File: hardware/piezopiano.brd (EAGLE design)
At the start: 175.5 x 99.8 mm, 75 parts, among them J1 CON2, J4 JST-PH-2-SMT-SE, Q1 DMN3404L, Q2 DMN3404L, Q3 DMN3404L, Q4 DMN3404L, Q5 DMN3404L, Q6 DMN3404L, Q7 DMN3404L, Q8 DMN3404L, U2 CH340E_MSOP10, U3 TP4333, U4 MEGA328PB-AU, Y1 830069392

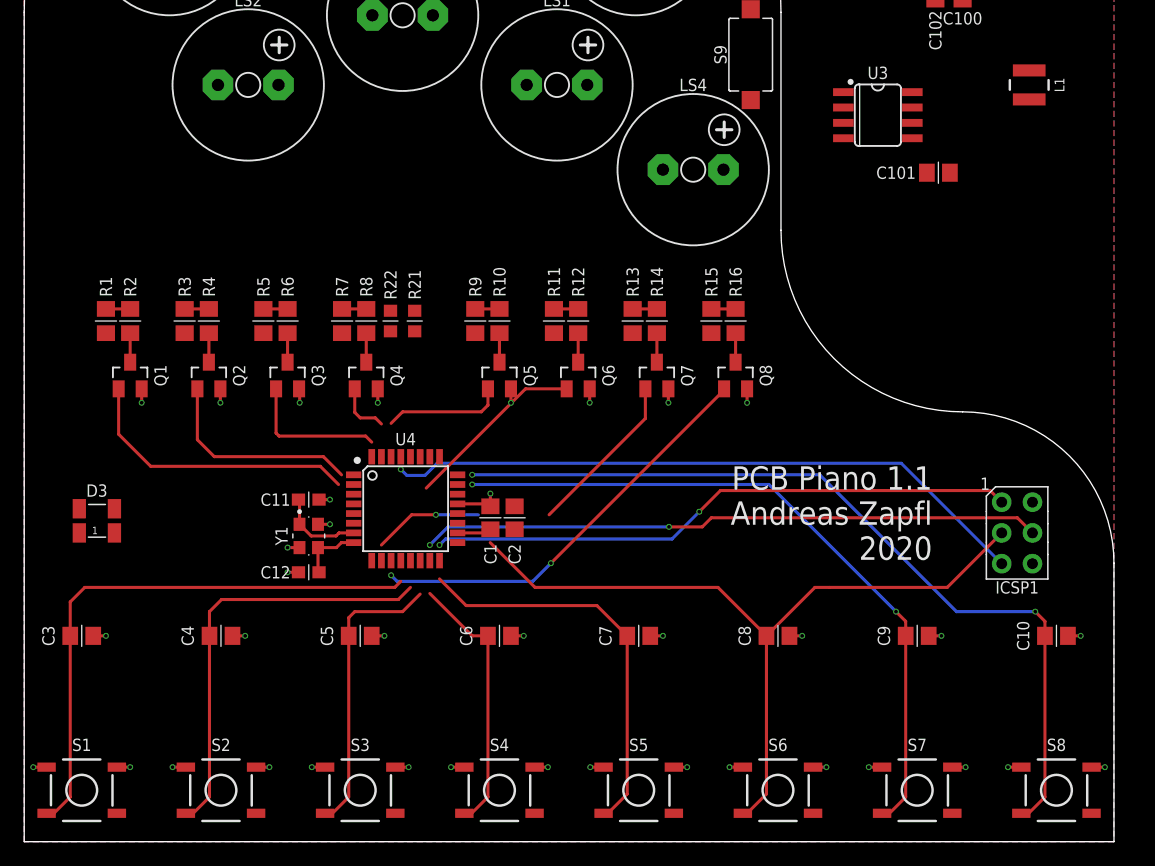
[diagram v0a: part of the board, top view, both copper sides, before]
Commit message: Added housing information and shifted piezo to be symmetric
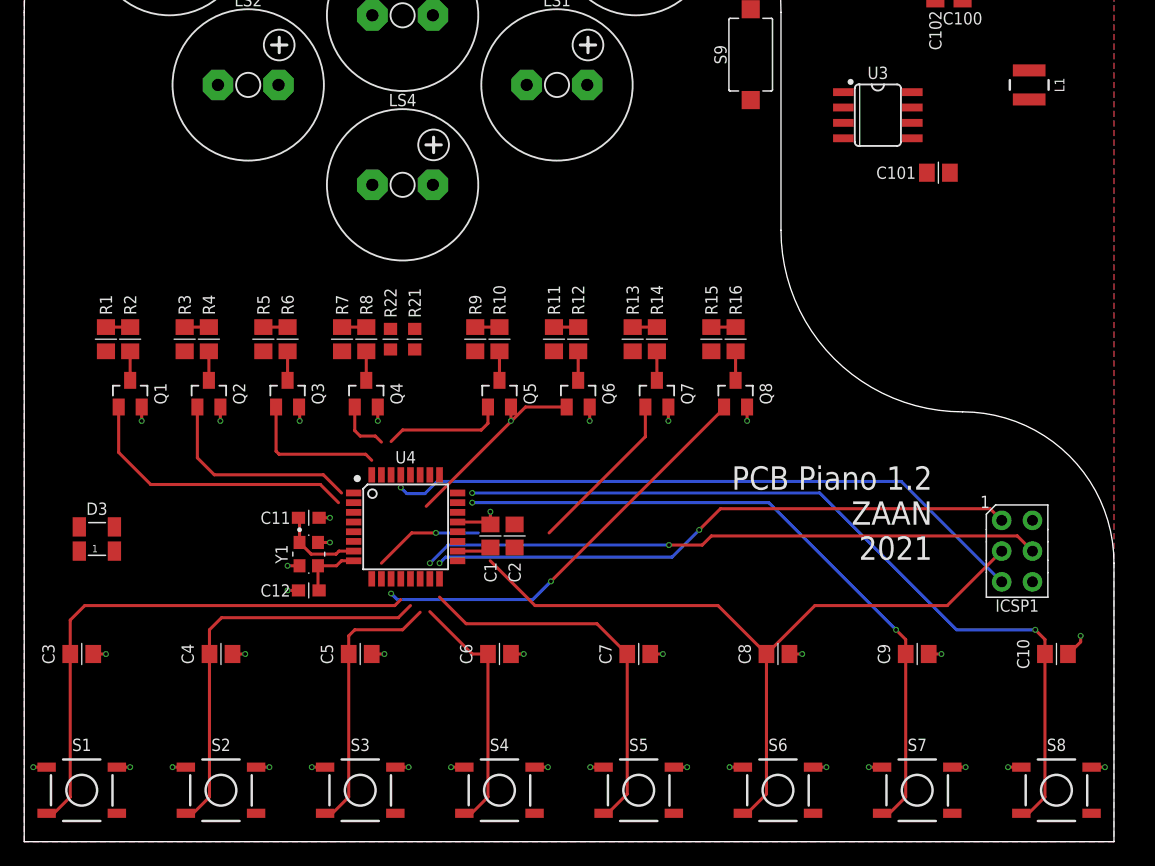
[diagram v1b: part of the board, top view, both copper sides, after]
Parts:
- moved LS4 24.0 mm to (31.2, 54.2)
- moved C1 1.50 mm to (38.5, 25.2)
- moved C10 1.50 mm to (85.2, 15.5)
- moved C11 1.50 mm to (23.5, 26.8)
- moved C12 1.50 mm to (23.5, 20.8)
- moved C2 1.50 mm to (40.5, 25.2)
- moved C3 1.50 mm to (4.75, 15.5)
- moved C4 1.50 mm to (16.2, 15.5)
- moved C5 1.50 mm to (27.8, 15.5)
- moved C6 1.50 mm to (39.2, 15.5)
- moved C7 1.50 mm to (50.8, 15.5)
- moved C8 1.50 mm to (62.2, 15.5)
- moved C9 1.50 mm to (73.8, 15.5)
- moved D3 1.50 mm to (6.00, 25.0)
- moved ICSP1 1.50 mm to (82.0, 24.0)
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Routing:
- net T7: track 64.6 -> 63.1 mm
- net T8: track 81.8 -> 80.3 mm
- net T6: track 57.5 -> 56.0 mm
- net T5: track 69.3 -> 67.8 mm
- net T4: track 46.6 -> 45.1 mm
- net T3: track 35.2 -> 33.7 mm
- net T2: track 24.0 -> 22.5 mm
- net T1: track 73.3 -> 71.8 mm
- net GND: track 42.9 -> 43.9 mm
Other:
- board text added: "PCB Piano 1.2 ZAAN 2021"
- board text removed: "PCB Piano 1.1 Andreas Zapfl 2020"

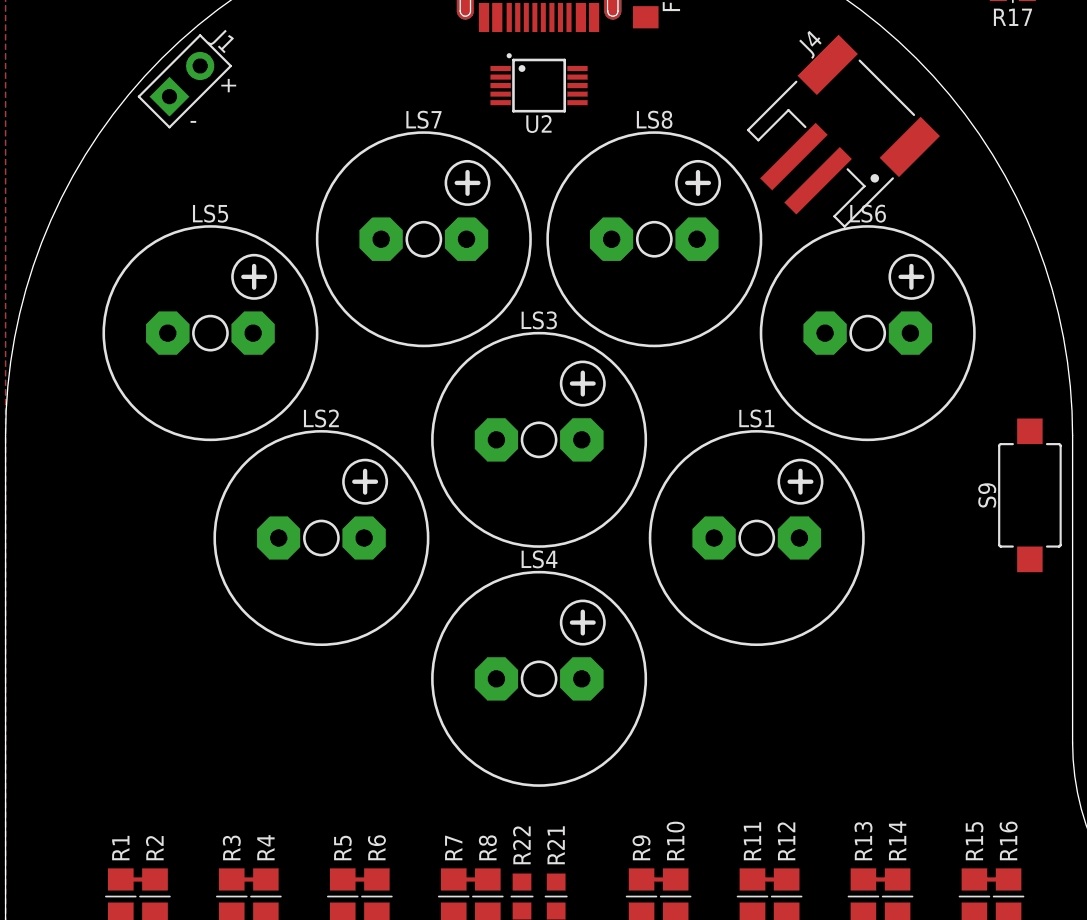
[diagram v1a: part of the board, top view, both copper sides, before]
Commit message: Mirrored piezos
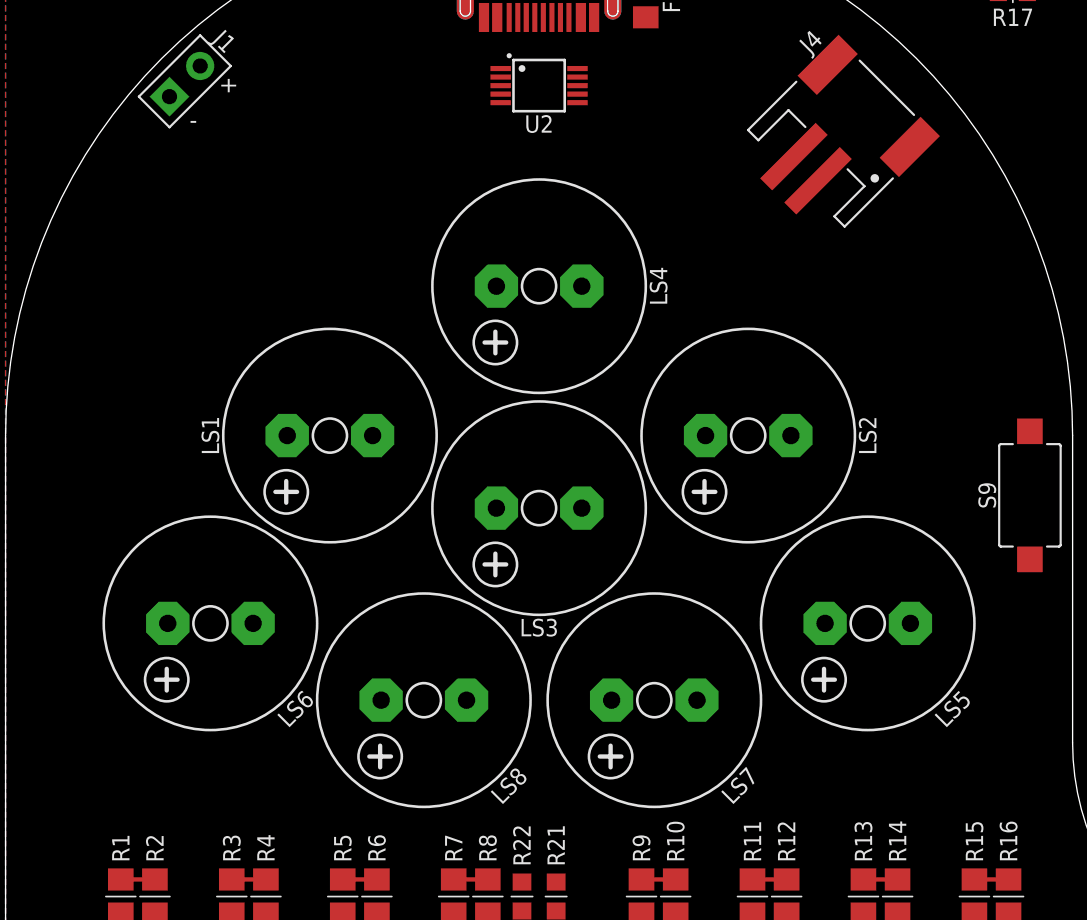
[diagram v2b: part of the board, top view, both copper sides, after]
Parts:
- moved LS5 42.1 mm to (50.5, 57.5), turned to 180 degrees
- moved LS6 42.1 mm to (12.0, 57.5), turned to 180 degrees
- moved LS7 30.2 mm to (38.0, 53.0), turned to 180 degrees
- moved LS8 30.2 mm to (24.5, 53.0), turned to 180 degrees
- moved LS1 25.7 mm to (19.0, 68.5), turned to 180 degrees
- moved LS2 25.7 mm to (43.5, 68.5), turned to 180 degrees
- moved LS4 23.0 mm to (31.2, 77.2), turned to 180 degrees
- moved LS3 4.00 mm to (31.2, 64.2), turned to 180 degrees

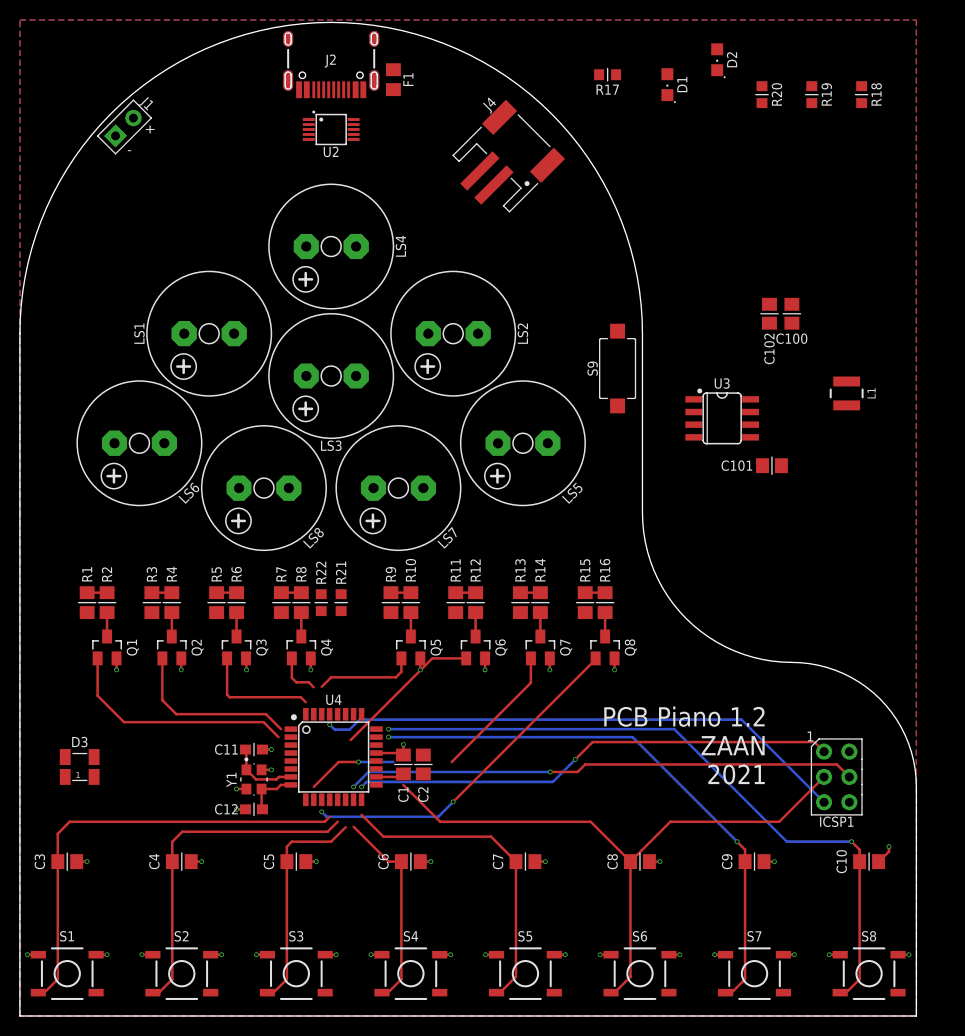
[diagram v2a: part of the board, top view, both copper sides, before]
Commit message: Added roundness to footprints
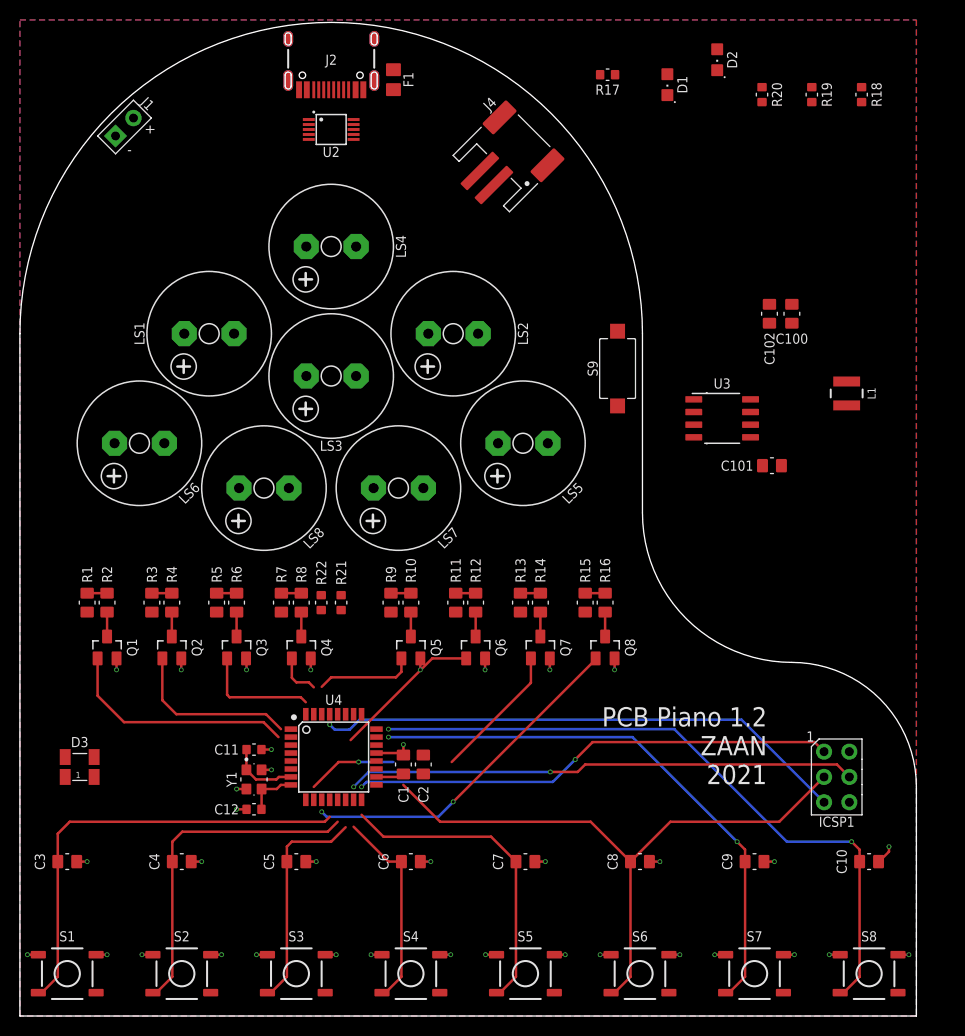
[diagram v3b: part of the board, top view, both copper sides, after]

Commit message: Changed ICSP
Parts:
- ICSP1: value AVRISP2.54MM -> AVR-ISP-SKEDD; device Custom:AVRISP-2.54 -> zaan-Connectors:490107670612_DEBUGGING
- moved ICSP1 5.85 mm to (76.5, 26.0), turned to 180 degrees
- moved C11 0.25 mm to (23.5, 26.5)
- moved C12 0.25 mm to (23.5, 21.0)
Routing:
- net T1: track 71.6 -> 44.6 mm
- net T8: track 80.3 -> 56.7 mm
- net T7: track 63.1 -> 40.2 mm
- net RST: track 53.7 -> 42.0 mm
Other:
- board text added: "- Prototype Area - WS LED - RGB LED"

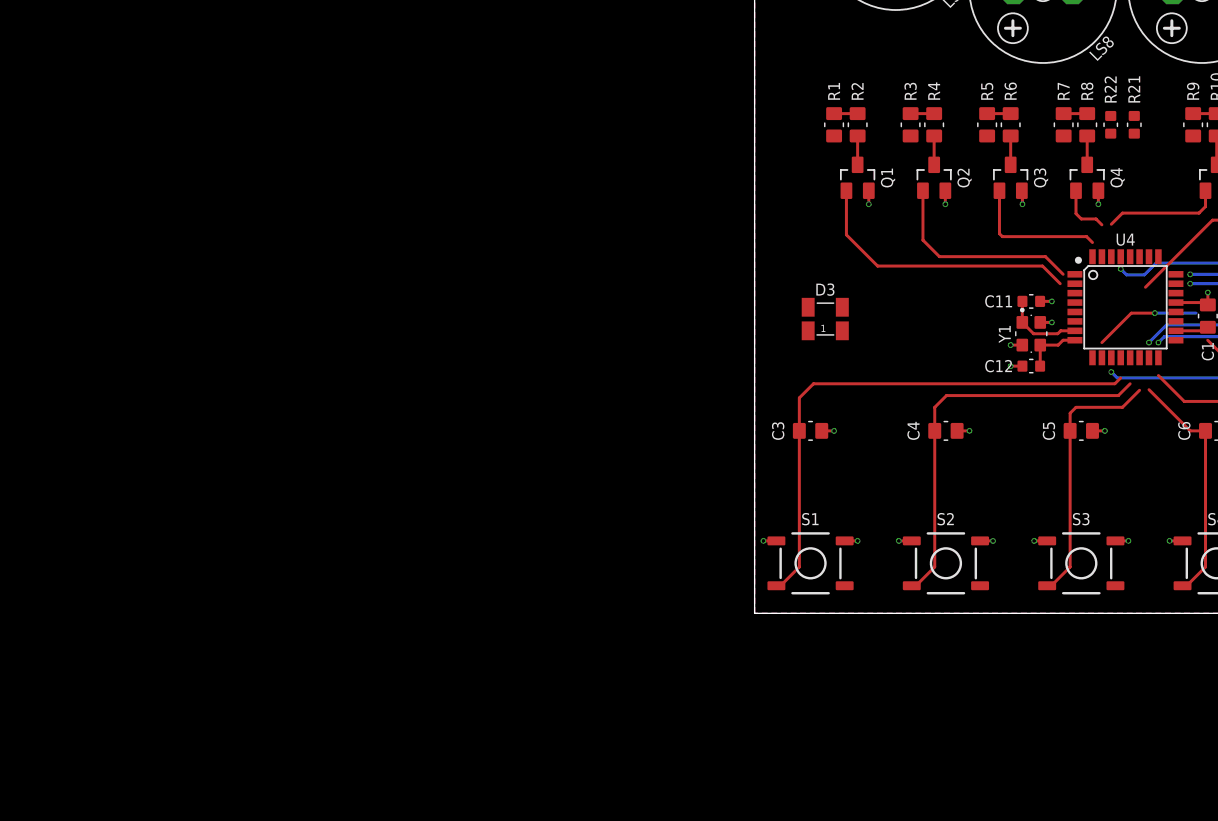
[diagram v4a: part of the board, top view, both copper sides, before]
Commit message: Changed pin naming at atmega328
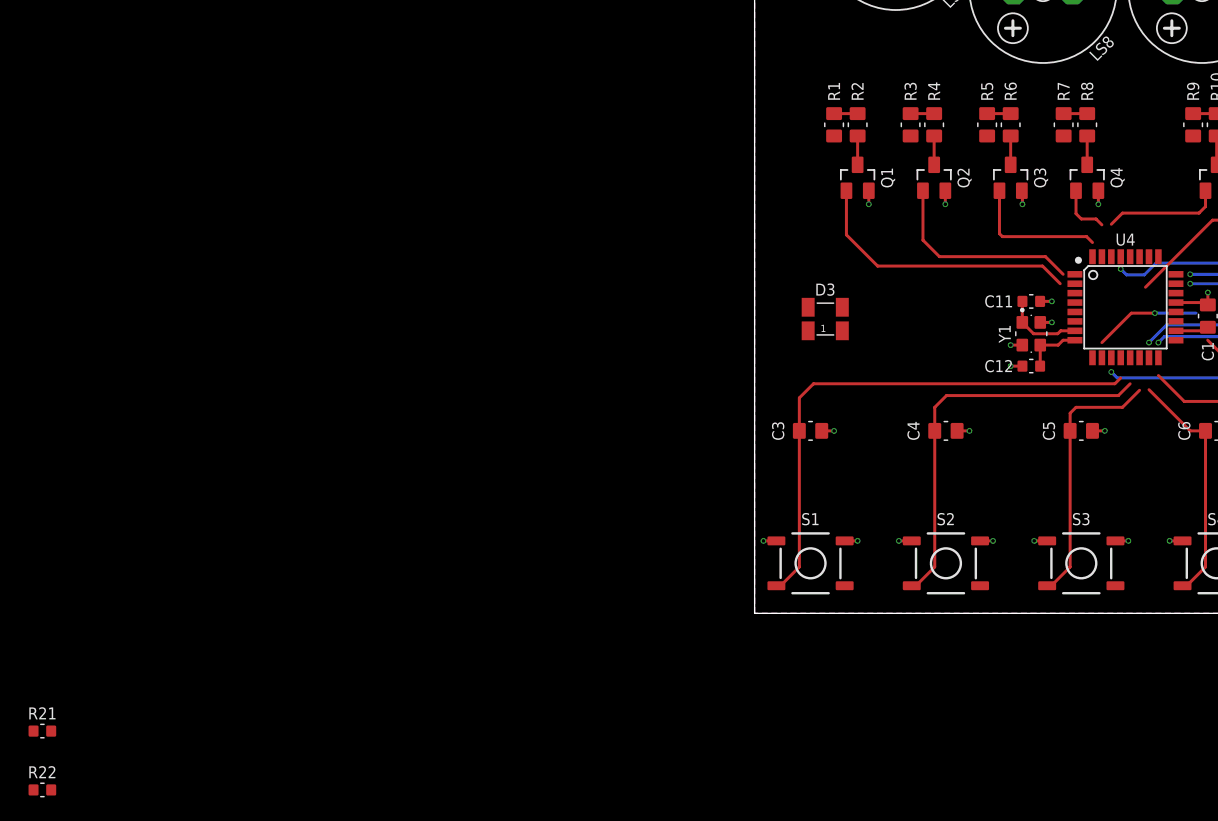
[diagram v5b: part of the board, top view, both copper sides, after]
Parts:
- moved R22 106.9 mm to (-60.5, -15.0), turned to 0 degrees
- moved R21 106.1 mm to (-60.5, -10.0), turned to 0 degrees
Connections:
- net N$19 renamed D0/RX
- net N$20 renamed D1/TX
- net NOTE1 renamed D2
- net NOTE3 renamed D4
- net NOTE4 renamed D3
- net NOTE6 renamed D5
- net NOTE7 renamed D7
- net NOTE8 renamed D6
- net T2 renamed D10
- net T3 renamed D9
- net T4 renamed D8
- net T5 renamed A1
- net T6 renamed A0
- new net A2: U4.25
- new net A3: U4.26
- new net A4: U4.27
- new net A5: U4.28
- new net D11/MOSI: U4.15
- new net D12/MISO: U4.16
- new net D13/SCK: U4.17

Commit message: Changed to 4809
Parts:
- removed C11, C12: 12p, zaan-Capacitors:C0603
- removed ICSP1: AVR-ISP-SKEDD, zaan-Connectors:490107670612_DEBUGGING
- removed U4: MEGA328PB-AU, zaan-IC-Microcontroller:TQFP32-08
- removed Y1: 830069392, zaan-Electromechanical:WE-XTAL_CFPX-218
- added C13: 100n, zaan-Capacitors:C0603
- added DBG1: AVR-UPDI-6-SKEDD, zaan-Connectors:490107670612_DEBUGGING
- added U$1: (no value), EET-Symbols:JLC_UID
- added U$2: (no value), EET-Symbols:QR-SPACE
- added U$3: (no value), EET-Symbols:STACKUP-2L
- added U1: ATMEGA4809, zaan-IC-Microcontroller:TQFP48
- C1, C2: device zaan-Capacitors:C0805 -> zaan-Capacitors:C0603
- moved R22 141.6 mm to (67.5, 45.5), turned to 90 degrees
- moved R21 138.1 mm to (66.0, 45.5), turned to 90 degrees
- moved C1 13.6 mm to (25.0, 27.0), turned to 270 degrees
- moved C2 10.1 mm to (33.0, 32.0), turned to 180 degrees
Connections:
- removed net A4: U4.27
- removed net A5: U4.28
- removed net D0/RX: R21.1, U4.30
- removed net D1/TX: R22.1, U4.31
- removed net D11/MOSI: U4.15
- removed net D12/MISO: U4.16
- removed net D13/SCK: U4.17
- removed net N$27: U4.4
- removed net RST: ICSP1.5, U4.29
- removed net XTAL1: C11.1, U4.7, Y1.1
- removed net XTAL2: C12.1, U4.8, Y1.3
- new net A4/SDA: U1.36, U1.46
- new net A5/SCL: U1.37, U1.47
- new net A6: U1.24
- new net A7: U1.25
- new net AREF: U1.27
- new net D10~: U1.5
- new net D3~: U1.39
- new net D5~: U1.6
- new net D6~: U1.38
- new net D9~: U1.4
- new net MISO: U1.31
- new net MOSI: U1.30
- new net N$35: U1.7
- new net N$39: U1.3
- new net N$40: U1.2
- new net N$41: U1.1
- new net N$44: U1.10
- new net N$45: U1.11
- new net N$46: U1.12
- new net N$47: U1.19
- new net N$51: U1.13
- new net N$56: U1.26
- new net N$60: U1.34
- new net N$61: U1.35
- new net N$71: U1.48
- new net RESETN: U1.40
- new net RX0: R21.1, U1.9
- new net RX1: U1.17
- new net SCK: U1.32
- new net TX0: R22.1, U1.8
- new net TX1: U1.16
- new net UDPI: DBG1.3, U1.41
- net +5V: now also C13.1, DBG1.4, U1.14, U1.28, U1.42; no longer ICSP1.2, U4.18
- net A0: now also U1.23; no longer U4.23
- net A1: now also U1.22; no longer U4.24
- net A2: now also U1.21; no longer U4.25
- net A3: now also U1.20; no longer U4.26
- net D10: no longer U4.14
- net D2: now also U1.44; no longer U4.32
- net D3: no longer U4.1
- net D4: now also U1.18; no longer U4.2
- net D5: no longer U4.9
- net D6: no longer U4.10
- net D7: now also U1.45; no longer U4.11
- net D8: now also U1.33; no longer U4.12
- net D9: no longer U4.13
- net GND: now also C13.2, DBG1.2, U1.15, U1.29, U1.43; no longer C11.2, C12.2, ICSP1.6, U4.21, Y1.2, Y1.4
- net N$28: now also DBG1.6; no longer U4.5
- net T1: no longer ICSP1.4
- net T7: no longer ICSP1.3
- net T8: no longer ICSP1.1
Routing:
- net RST: track 42.0 -> 0.00 mm, vias 1 -> 0
- net D7: track 34.4 -> 0.00 mm, vias 2 -> 0
- net T8: track 56.7 -> 31.6 mm, vias 2 -> 0
- net T1: track 44.6 -> 20.4 mm, vias 2 -> 0
- net D6: track 22.7 -> 0.00 mm, vias 1 -> 0
- net D2: track 11.9 -> 4.57 mm
- net XTAL1: track 6.76 -> 0.00 mm
- net D3: track 17.3 -> 10.6 mm
- net D4: track 23.6 -> 16.9 mm
- net D8: track 45.0 -> 39.5 mm
- net D9: track 33.6 -> 28.3 mm
- net D5: track 15.1 -> 9.99 mm
- net XTAL2: track 4.90 -> 0.00 mm
- net +5V: track 2.83 -> 5.80 mm
- net GND: track 44.1 -> 44.0 mm, vias 37 -> 35
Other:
- board size 175.5 x 99.8 mm -> 90 x 99.8 mm
